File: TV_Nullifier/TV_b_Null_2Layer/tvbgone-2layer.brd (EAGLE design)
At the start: 18 x 42.4 mm, 18 parts, among them IC1 ATTINY85V-10S, Q1 BC857AT115, Q2 PMBT3904VS_DUAL_NPN, Y1_8MHZ RESONATOR

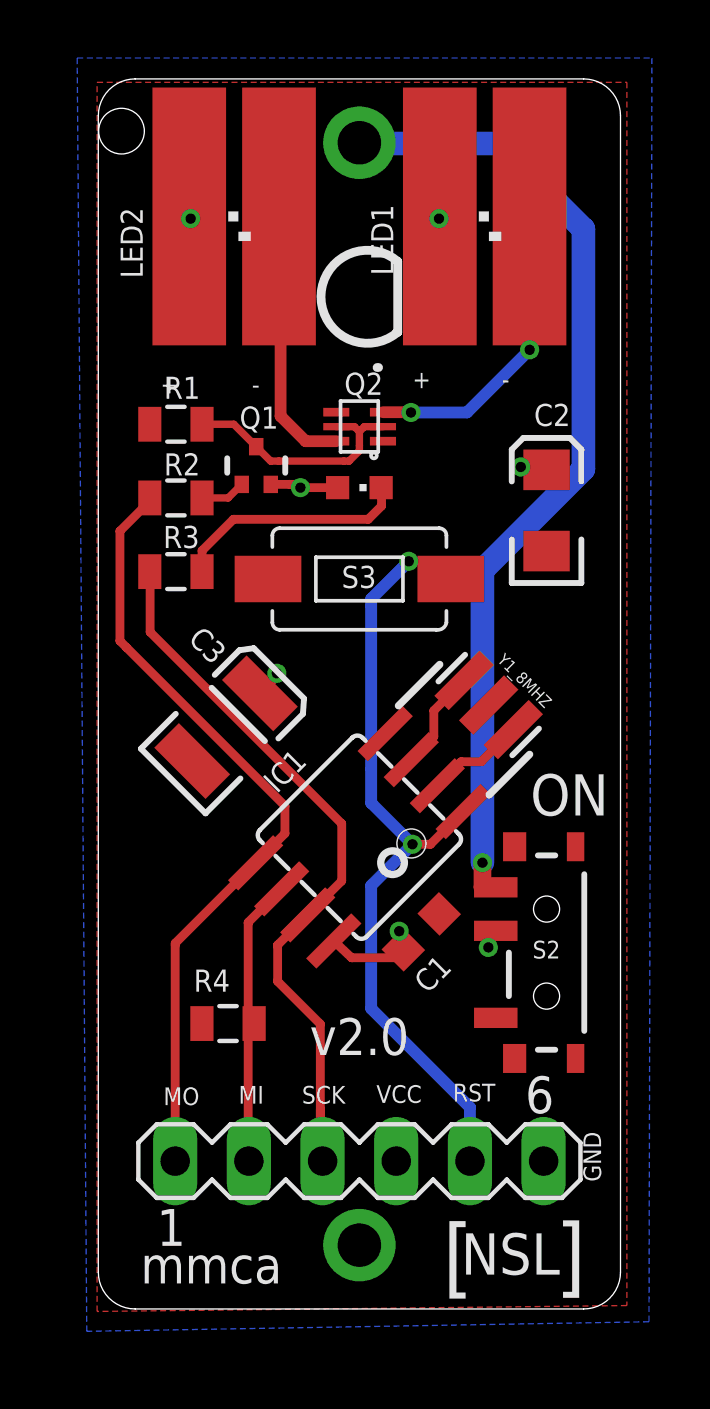
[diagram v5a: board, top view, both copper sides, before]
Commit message: 
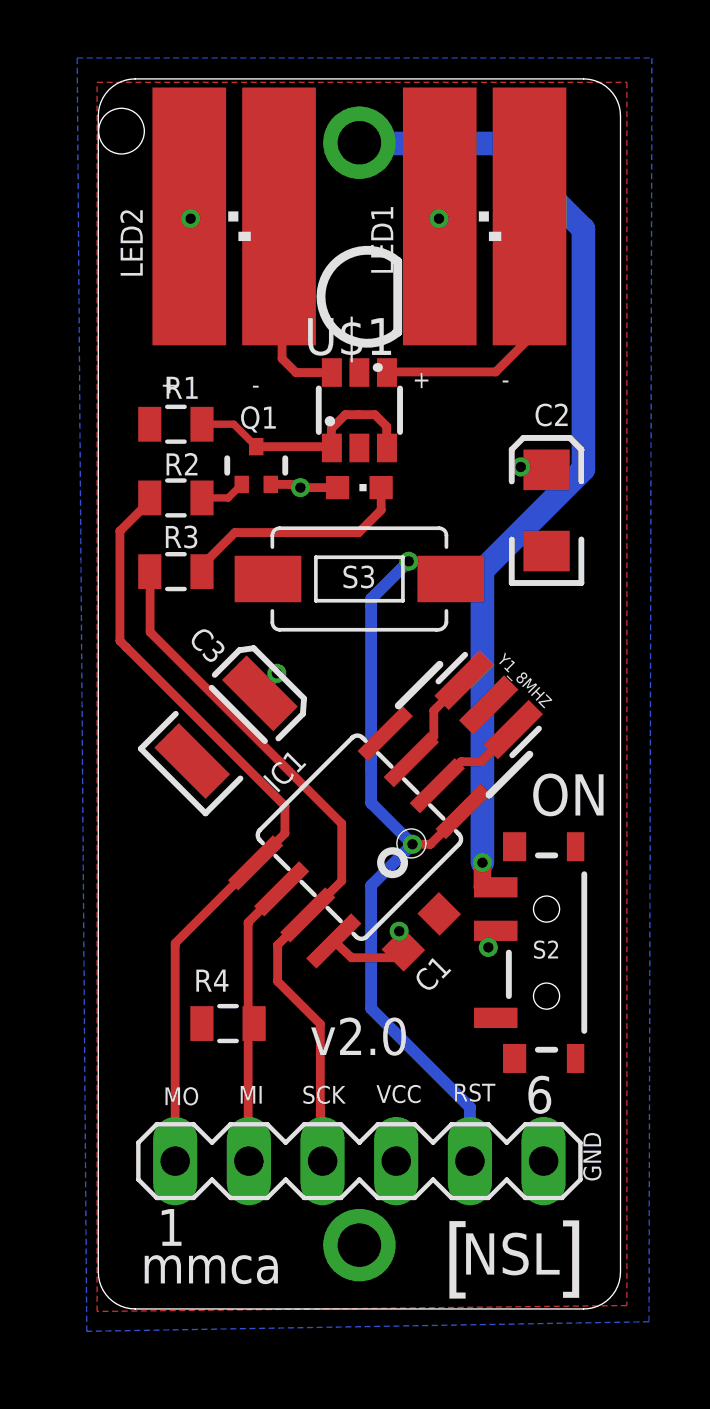
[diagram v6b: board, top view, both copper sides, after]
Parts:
- removed Q2: PMBT3904VS_DUAL_NPN, tvbgone-2layer:SOT666
- added U$1: DUALNPN, 6x6:SSOT6
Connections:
- net GND: now also U$1.2, U$1.5; no longer Q2.1, Q2.4
- net N$4: now also U$1.4; no longer Q2.3
- net N$5: now also U$1.6; no longer Q2.6
- net N$9: now also U$1.1, U$1.3; no longer Q2.2, Q2.5
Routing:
- net N$5: track 9.16 -> 6.87 mm
- net N$4: track 10.6 -> 9.60 mm, vias 2 -> 0
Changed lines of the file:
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@@
 <layer number="106" name="bPlate" color="7" fill="1" visible="no" active="yes"/>
 <layer number="107" name="Crop" color="7" fill="1" visible="no" active="yes"/>
+<layer number="108" name="fp8" color="7" fill="1" visible="yes" active="yes"/>
+<layer number="109" name="fp9" color="7" fill="1" visible="yes" active="yes"/>
+<layer number="110" name="fp0" color="7" fill="1" visible="yes" active="yes"/>
 <layer number="116" name="Patch_BOT" color="9" fill="4" visible="no" active="yes"/>
 <layer number="121" name="_tsilk" color="7" fill="1" visible="no" active="yes"/>
 <layer number="122" name="_bsilk" color="7" fill="1" visible="no" active="yes"/>
+<layer number="123" name="tTestmark" color="7" fill="1" visible="yes" active="yes"/>
+<layer number="124" name="bTestmark" color="7" fill="1" visible="yes" active="yes"/>
 <layer number="125" name="_tNames" color="7" fill="1" visible="no" active="yes"/>
+<layer number="131" name="prix" color="7" fill="1" visible="yes" active="yes"/>
+<layer number="132" name="test" color="7" fill="1" visible="yes" active="yes"/>
 <layer number="144" name="Drill_legend" color="7" fill="1" visible="no" active="yes"/>
 <layer number="151" name="HeatSink" color="7" fill="1" visible="no" active="yes"/>
+<layer number="199" name="Contour" color="7" fill="1" visible="yes" active="yes"/>
 <layer number="200" name="200bmp" color="1" fill="10" visible="no" active="no"/>
 <layer number="201" name="201bmp" color="2" fill="10" visible="no" active="yes"/>
@@
 <attribute name="VALUE" x="-3" y="1.2624" size="0.762" layer="27"/>
 </element>
-<element name="Q2" library="tvbgone-2layer" package="SOT666" value="PMBT3904VS_DUAL_NPN" x="0" y="9.2202" smashed="yes" rot="R90">
-<attribute name="NAME" x="0.8174" y="11.0726" size="0.762" layer="21" font="vector" rot="R180"/>
-</element>
 <element name="C3" library="tvbgone-2layer" package="SPARKFUN_EIA3528" value="" x="-4.59665" y="-1.14555" smashed="yes" rot="R45">
 <attribute name="NAME" x="-4.51635625" y="1.50749375" size="0.762" layer="21" font="vector" rot="R135"/>
 <attribute name="VALUE" x="-1.3368875" y="0.176740625" size="1.27" layer="27" rot="R135"/>
 </element>
+<element name="U$1" library="6x6" package="SSOT6" value="DUALNPN" x="0" y="9.779"/>
 </elements>
 <signals>
@@
 </polygon>
 <contactref element="S3" pad="P$1"/>
-<contactref element="Q2" pad="1"/>
-<contactref element="Q2" pad="4"/>
 <contactref element="C3" pad="C"/>
+<contactref element="U$1" pad="5"/>
+<contactref element="U$1" pad="2"/>
 </signal>
 <signal name="N$1">
@@
 <contactref element="LED3" pad="C"/>
 <contactref element="R3" pad="2"/>
-<wire x1="-5.4246" y1="4.2164" x2="-5.4246" y2="4.9386" width="0.3048" layer="1"/>
-<wire x1="-5.4246" y1="4.9386" x2="-4.3434" y2="6.0198" width="0.3048" layer="1"/>
-<wire x1="-4.3434" y1="6.0198" x2="0.3048" y2="6.0198" width="0.3048" layer="1"/>
-<wire x1="0.3048" y1="6.0198" x2="0.762" y2="6.477" width="0.3048" layer="1"/>
-<wire x1="0.762" y1="6.477" x2="0.762" y2="7.1" width="0.3048" layer="1"/>
 <wire x1="0.762" y1="7.1" x2="0.75" y2="7.112" width="0.3048" layer="1"/>
+<wire x1="-0.0254" y1="5.5626" x2="0.75" y2="6.338" width="0.3048" layer="1"/>
+<wire x1="0.75" y1="6.338" x2="0.75" y2="7.112" width="0.3048" layer="1"/>
+<wire x1="-5.4246" y1="4.2164" x2="-5.4246" y2="4.4306" width="0.3048" layer="1"/>
+<wire x1="-5.4246" y1="4.4306" x2="-4.2926" y2="5.5626" width="0.3048" layer="1"/>
+<wire x1="-4.2926" y1="5.5626" x2="-0.0254" y2="5.5626" width="0.3048" layer="1"/>
 </signal>
 <signal name="MOSI">
@@
 <signal name="N$4">
 <contactref element="LED1" pad="C"/>
-<contactref element="Q2" pad="3"/>
-<wire x1="0.8128" y1="9.7122" x2="1.7686" y2="9.7122" width="0.4064" layer="1"/>
-<wire x1="1.7686" y1="9.7122" x2="1.778" y2="9.7028" width="0.4064" layer="1"/>
-<via x="1.778" y="9.7028" extent="1-16" drill="0.3556"/>
-<wire x1="1.778" y1="9.7028" x2="3.7084" y2="9.7028" width="0.4064" layer="16"/>
-<wire x1="3.7084" y1="9.7028" x2="5.8674" y2="11.8618" width="0.4064" layer="16"/>
-<via x="5.8674" y="11.8618" extent="1-16" drill="0.3556"/>
-<wire x1="5.8674" y1="11.8618" x2="5.8674" y2="16.4566" width="0.4064" layer="1"/>
-<wire x1="5.8674" y1="16.4566" x2="5.8648" y2="16.4592" width="0.4064" layer="1"/>
+<contactref element="U$1" pad="4"/>
+<wire x1="0.95" y1="11.079" x2="0.9708" y2="11.0998" width="0.3048" layer="1"/>
+<wire x1="0.9708" y1="11.0998" x2="4.699" y2="11.0998" width="0.3048" layer="1"/>
+<wire x1="4.699" y1="11.0998" x2="5.8648" y2="12.2656" width="0.3048" layer="1"/>
+<wire x1="5.8648" y1="12.2656" x2="5.8648" y2="16.4592" width="0.3048" layer="1"/>
 </signal>
 <signal name="N$5">
 <contactref element="LED2" pad="C"/>
-<contactref element="Q2" pad="6"/>
 <wire x1="-2.7178" y1="15.2374" x2="-2.7712" y2="16.4592" width="0.3048" layer="1"/>
-<wire x1="-0.7972" y1="8.7122" x2="-1.8542" y2="8.7122" width="0.4064" layer="1"/>
-<wire x1="-1.8542" y1="8.7122" x2="-2.7178" y2="9.5758" width="0.4064" layer="1"/>
-<wire x1="-2.7178" y1="9.5758" x2="-2.7178" y2="15.2374" width="0.4064" layer="1"/>
+<contactref element="U$1" pad="6"/>
+<wire x1="-2.7178" y1="15.2374" x2="-2.667" y2="15.2374" width="0.3048" layer="1"/>
+<wire x1="-2.667" y1="15.2374" x2="-2.667" y2="11.557" width="0.3048" layer="1"/>
+<wire x1="-2.667" y1="11.557" x2="-2.189" y2="11.079" width="0.3048" layer="1"/>
+<wire x1="-2.189" y1="11.079" x2="-0.95" y2="11.079" width="0.3048" layer="1"/>
 </signal>
 <signal name="N$8">
@@
 <contactref element="Q1" pad="1"/>
 <contactref element="R1" pad="1"/>
-<contactref element="Q2" pad="2"/>
-<contactref element="Q2" pad="5"/>
-<wire x1="-2.779" y1="8.0264" x2="-0.5334" y2="8.0264" width="0.254" layer="1"/>
-<wire x1="0" y1="8.5598" x2="0" y2="9.0424" width="0.254" layer="1"/>
-<wire x1="0" y1="9.0424" x2="-0.1698" y2="9.2122" width="0.254" layer="1"/>
-<wire x1="-0.1698" y1="9.2122" x2="-0.7972" y2="9.2122" width="0.254" layer="1"/>
-<wire x1="0.8128" y1="9.2122" x2="0.1698" y2="9.2122" width="0.254" layer="1"/>
-<wire x1="0.1698" y1="9.2122" x2="0" y2="9.0424" width="0.254" layer="1"/>
-<wire x1="-0.5334" y1="8.0264" x2="-0.3556" y2="8.0264" width="0.254" layer="1"/>
-<wire x1="-0.3556" y1="8.0264" x2="0" y2="8.382" width="0.254" layer="1"/>
-<wire x1="0" y1="8.382" x2="0" y2="8.5598" width="0.254" layer="1"/>
-<wire x1="-2.779" y1="8.0264" x2="-3.0584" y2="8.0264" width="0.254" layer="1"/>
-<wire x1="-3.0584" y1="8.0264" x2="-3.556" y2="8.524" width="0.254" layer="1"/>
 <wire x1="-5.4246" y1="9.2964" x2="-4.3284" y2="9.2964" width="0.254" layer="1"/>
 <wire x1="-4.3284" y1="9.2964" x2="-3.556" y2="8.524" width="0.254" layer="1"/>
+<contactref element="U$1" pad="1"/>
+<contactref element="U$1" pad="3"/>
+<wire x1="-3.556" y1="8.524" x2="-0.95" y2="8.524" width="0.3048" layer="1"/>
+<wire x1="-0.95" y1="8.524" x2="-0.95" y2="8.479" width="0.3048" layer="1"/>
+<wire x1="-0.95" y1="8.479" x2="-0.9652" y2="8.4942" width="0.3048" layer="1"/>
+<wire x1="-0.9652" y1="8.4942" x2="-0.9652" y2="9.144" width="0.3048" layer="1"/>
+<wire x1="-0.9652" y1="9.144" x2="-0.4826" y2="9.6266" width="0.3048" layer="1"/>
+<wire x1="-0.4826" y1="9.6266" x2="-0.0254" y2="9.6266" width="0.3048" layer="1"/>
+<wire x1="-0.0254" y1="9.6266" x2="0.5334" y2="9.6266" width="0.3048" layer="1"/>
+<wire x1="0.5334" y1="9.6266" x2="0.9398" y2="9.2202" width="0.3048" layer="1"/>
+<wire x1="0.9398" y1="9.2202" x2="0.9398" y2="8.4892" width="0.3048" layer="1"/>
+<wire x1="0.9398" y1="8.4892" x2="0.95" y2="8.479" width="0.3048" layer="1"/>
 </signal>
 </signals>

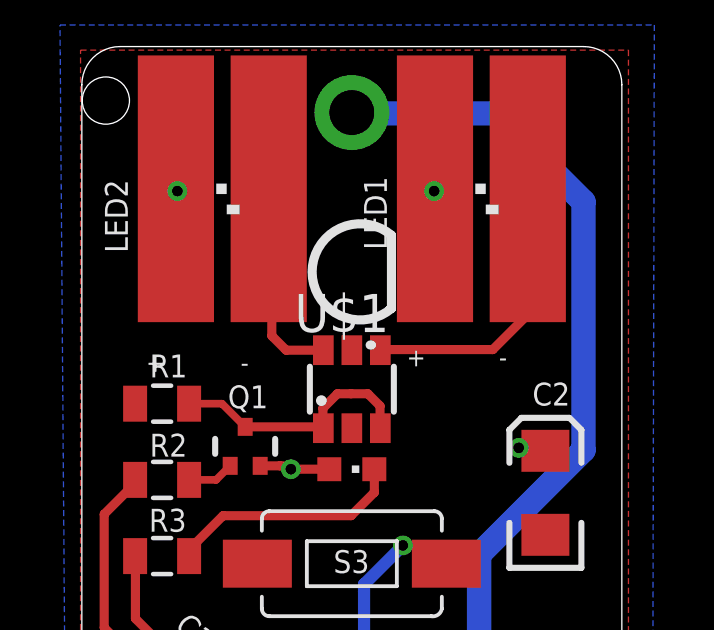
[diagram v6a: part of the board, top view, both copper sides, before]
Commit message: 
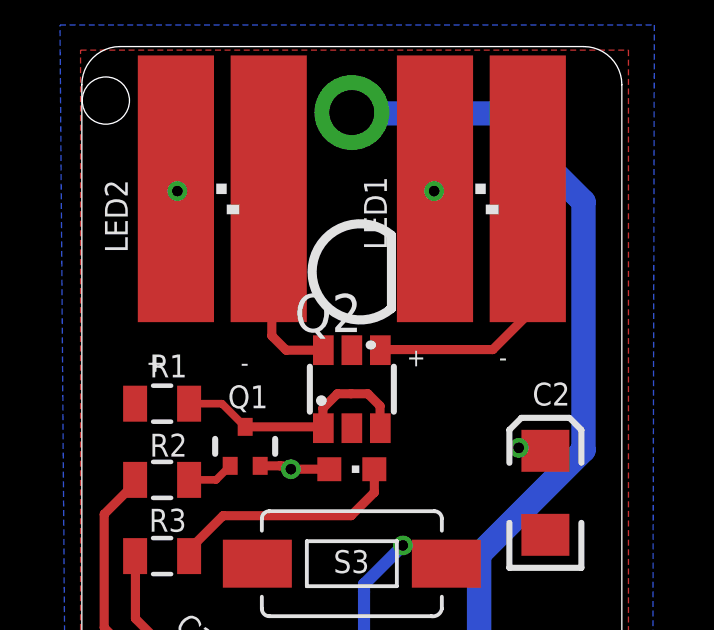
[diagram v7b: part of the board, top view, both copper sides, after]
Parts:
- renumbered U$1 to Q2
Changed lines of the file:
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@@
 <attribute name="VALUE" x="-1.3368875" y="0.176740625" size="1.27" layer="27" rot="R135"/>
 </element>
-<element name="U$1" library="6x6" package="SSOT6" value="DUALNPN" x="0" y="9.779"/>
+<element name="Q2" library="6x6" package="SSOT6" value="DUALNPN" x="0" y="9.779"/>
 </elements>
 <signals>
@@
 <contactref element="S3" pad="P$1"/>
 <contactref element="C3" pad="C"/>
-<contactref element="U$1" pad="5"/>
-<contactref element="U$1" pad="2"/>
+<contactref element="Q2" pad="5"/>
+<contactref element="Q2" pad="2"/>
 </signal>
 <signal name="N$1">
@@
 <signal name="N$4">
 <contactref element="LED1" pad="C"/>
-<contactref element="U$1" pad="4"/>
+<contactref element="Q2" pad="4"/>
 <wire x1="0.95" y1="11.079" x2="0.9708" y2="11.0998" width="0.3048" layer="1"/>
 <wire x1="0.9708" y1="11.0998" x2="4.699" y2="11.0998" width="0.3048" layer="1"/>
@@
 <contactref element="LED2" pad="C"/>
 <wire x1="-2.7178" y1="15.2374" x2="-2.7712" y2="16.4592" width="0.3048" layer="1"/>
-<contactref element="U$1" pad="6"/>
+<contactref element="Q2" pad="6"/>
 <wire x1="-2.7178" y1="15.2374" x2="-2.667" y2="15.2374" width="0.3048" layer="1"/>
 <wire x1="-2.667" y1="15.2374" x2="-2.667" y2="11.557" width="0.3048" layer="1"/>
@@
 <wire x1="-5.4246" y1="9.2964" x2="-4.3284" y2="9.2964" width="0.254" layer="1"/>
 <wire x1="-4.3284" y1="9.2964" x2="-3.556" y2="8.524" width="0.254" layer="1"/>
-<contactref element="U$1" pad="1"/>
-<contactref element="U$1" pad="3"/>
+<contactref element="Q2" pad="1"/>
+<contactref element="Q2" pad="3"/>
 <wire x1="-3.556" y1="8.524" x2="-0.95" y2="8.524" width="0.3048" layer="1"/>
 <wire x1="-0.95" y1="8.524" x2="-0.95" y2="8.479" width="0.3048" layer="1"/>
